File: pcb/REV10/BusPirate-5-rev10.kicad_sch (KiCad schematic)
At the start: 10 parts

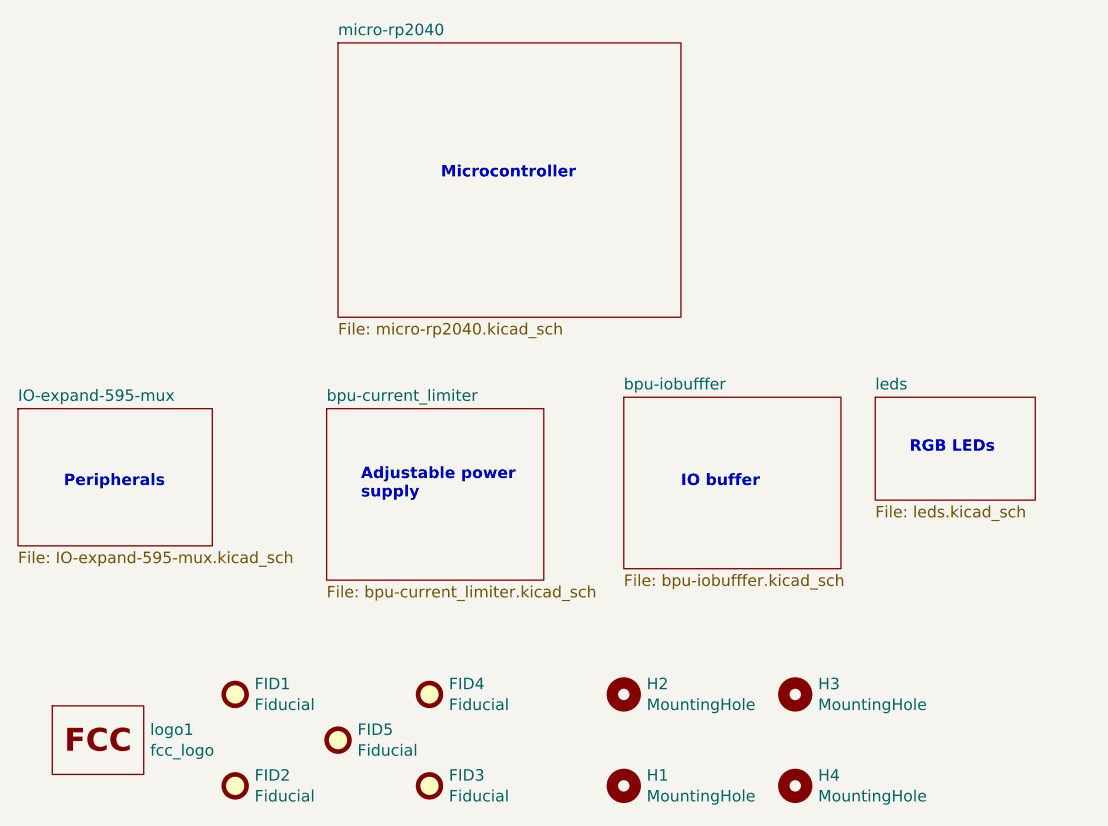
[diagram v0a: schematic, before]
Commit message: Add pulldown on VREF. Change VUSB MUX series resistor to 510R. May be other value updates that didn't get checked in previously.
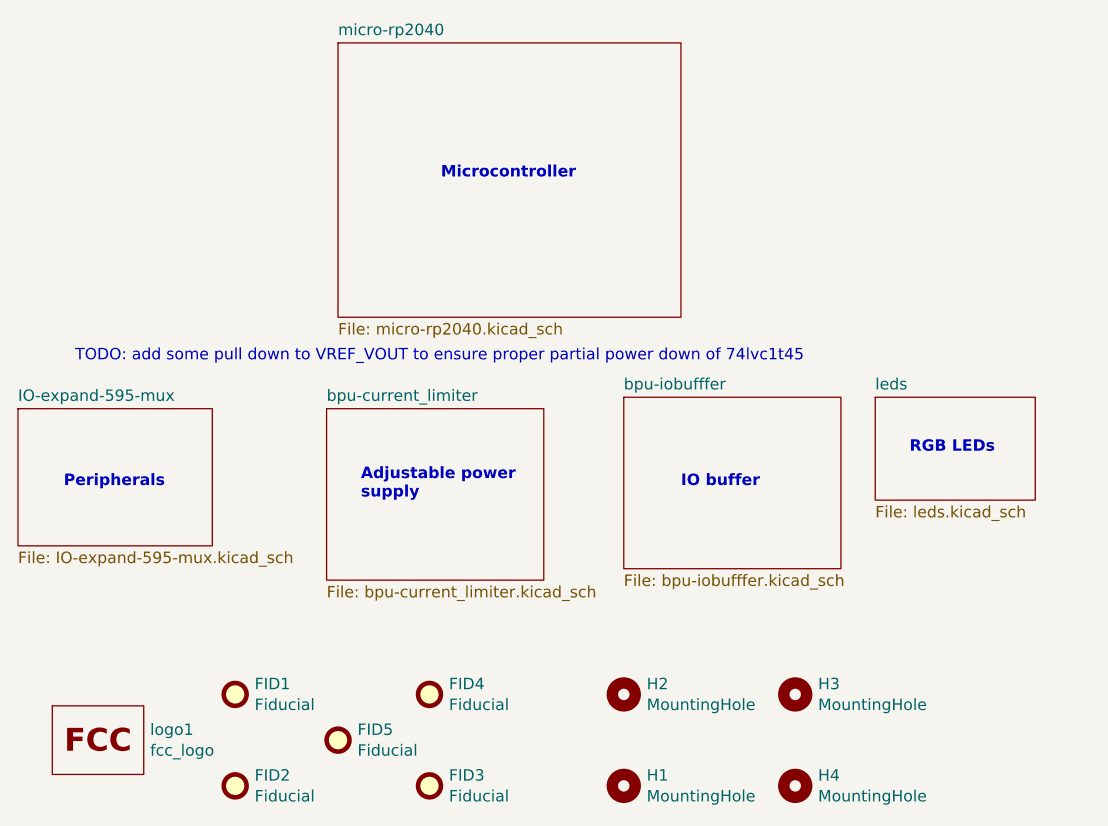
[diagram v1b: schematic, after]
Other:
- note added: "TODO: add some pull down to VREF_VOUT to ensure proper partial power down of 74lvc1t45"
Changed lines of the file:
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@@
     (effects (font (size 1.27 1.27) (thickness 0.254) bold) (justify left bottom))
+  )
+  (text "TODO: add some pull down to VREF_VOUT to ensure proper partial power down of 74lvc1t45"
+    (at 91.44 80.01 0)
+    (effects (font (size 1.27 1.27)) (justify left bottom))
   )
   (text "IO buffer" (at 158.75 93.98 0)
